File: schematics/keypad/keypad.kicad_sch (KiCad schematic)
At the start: 85 parts, among them J1 BOARD, J2 PRG, SW1 cherry_mx_rgb, SW10 cherry_mx_rgb, SW11 cherry_mx_rgb, SW12 cherry_mx_rgb, SW13 cherry_mx_rgb, SW14 cherry_mx_rgb, SW15 cherry_mx_rgb, SW16 cherry_mx_rgb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

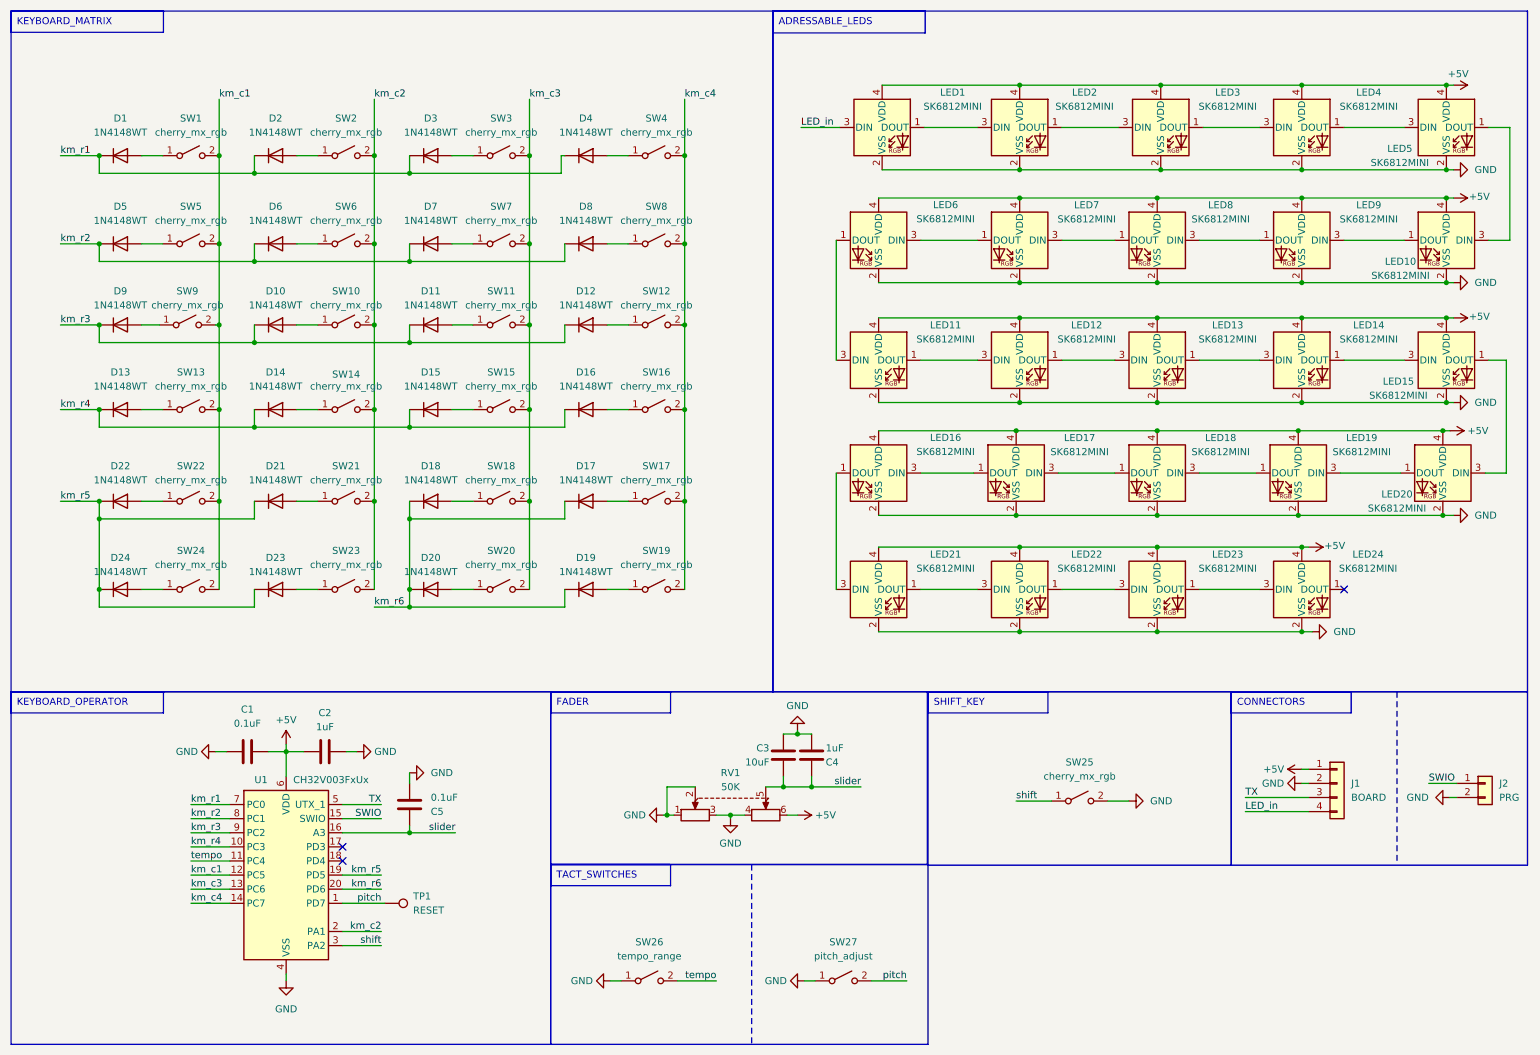
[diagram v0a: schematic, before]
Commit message: chore(hw): migrate keypad to KiCad v9
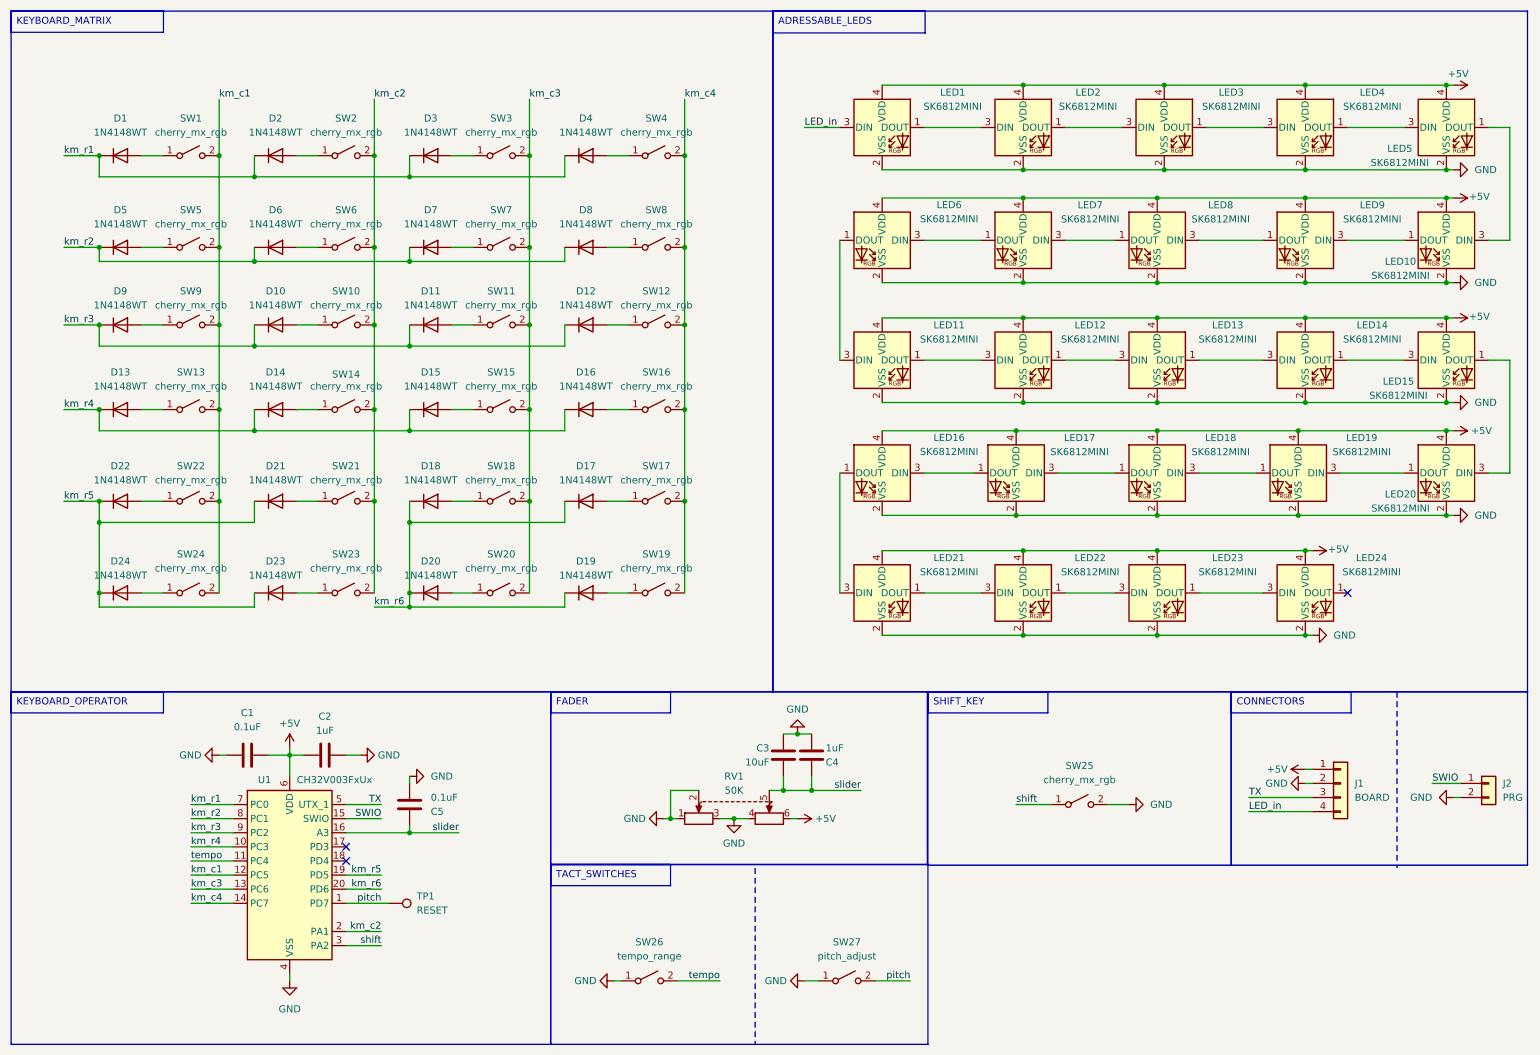
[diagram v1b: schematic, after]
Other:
- company: (none) -> Author: Kacper Jelonek
- title: (none) -> KEYPAD_AND_SLIDER
- moved on the sheet: C1, C2, D19, D20, D23, D24, D5, D6, D7, D8, J1, J2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

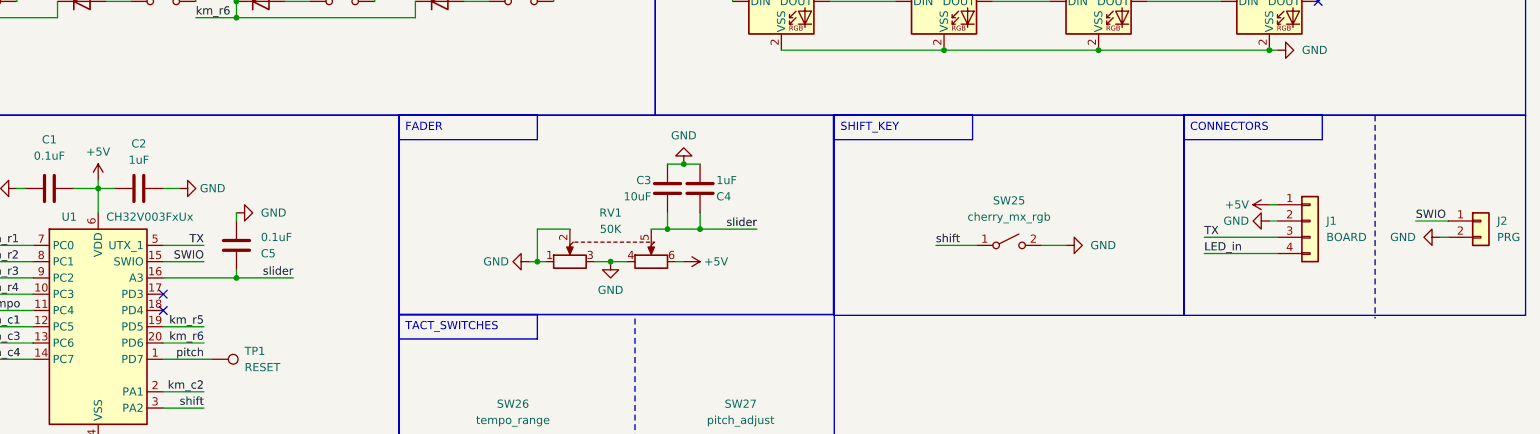
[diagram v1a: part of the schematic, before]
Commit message: hw: add encoder support to keypad
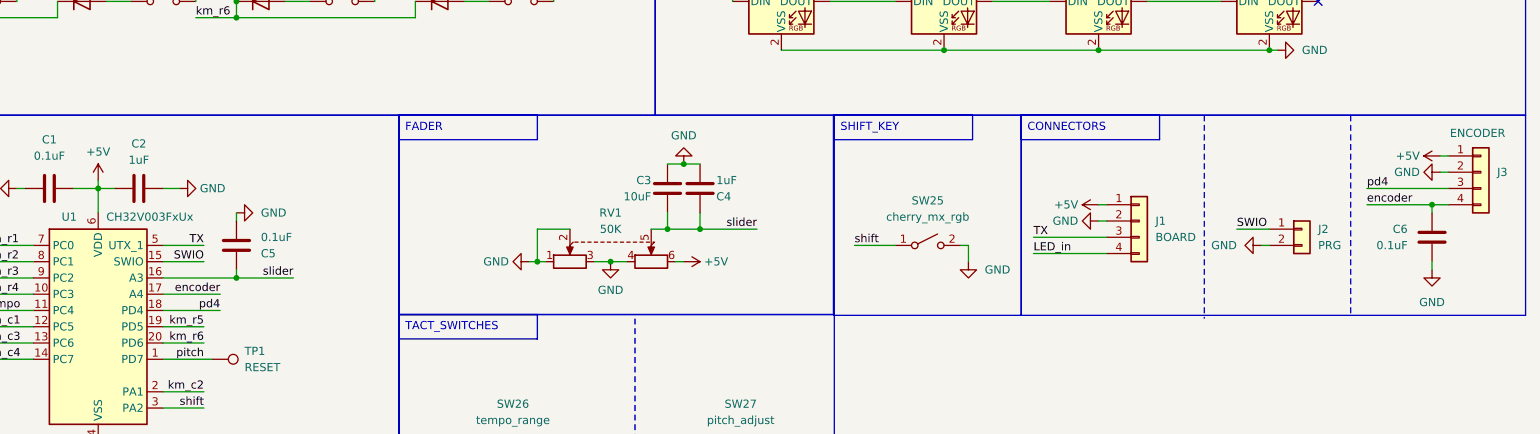
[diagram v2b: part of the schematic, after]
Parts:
- added C6: 0.1uF, Capacitor_SMD:C_0603_1608Metric, symbol Device:C
- added J3: ENCODER, Connector_PinHeader_2.54mm:PinHeader_1x04_P2.54mm_Vertical, symbol PCM_4ms_Connector:Conn_01x04
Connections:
- net +5V: now also J3.1 (Pin_1)
- net GND: now also C6.1, J3.2 (Pin_2)
- net encoder: now reaches U1.17 (PD3)
- net encoder: now also C6.2, J3.4 (Pin_4)
- net pd4: now reaches U1.18 (PD4)
- net pd4: now also J3.3 (Pin_3)
- no-connect marks 3 -> 1
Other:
- moved on the sheet: J1, J2, SW25
